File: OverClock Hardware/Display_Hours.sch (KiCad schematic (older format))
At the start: 41 parts

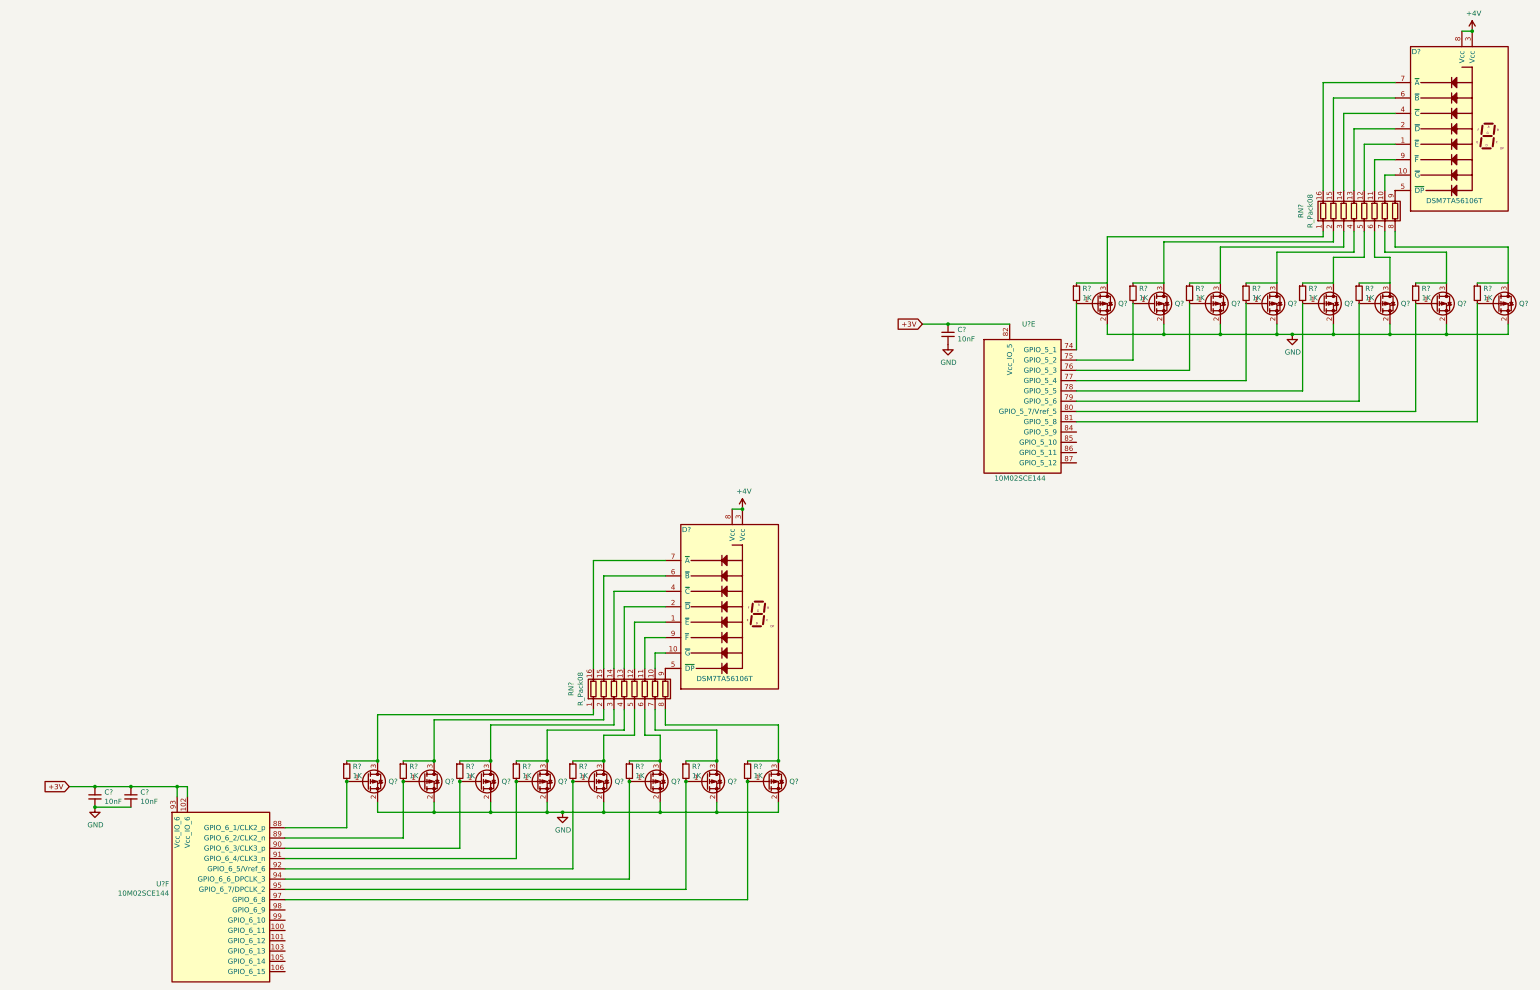
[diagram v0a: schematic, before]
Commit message: Interfaced minutes digits to FPGA and added time selection methods
Interfaced the two 7 Segment displays used for displaying the minutes to the FPGA. 

Added 4 Tactile switches to increment/decrement the hours and minutes separately.

Added a header to allow for setting of the time via UART.
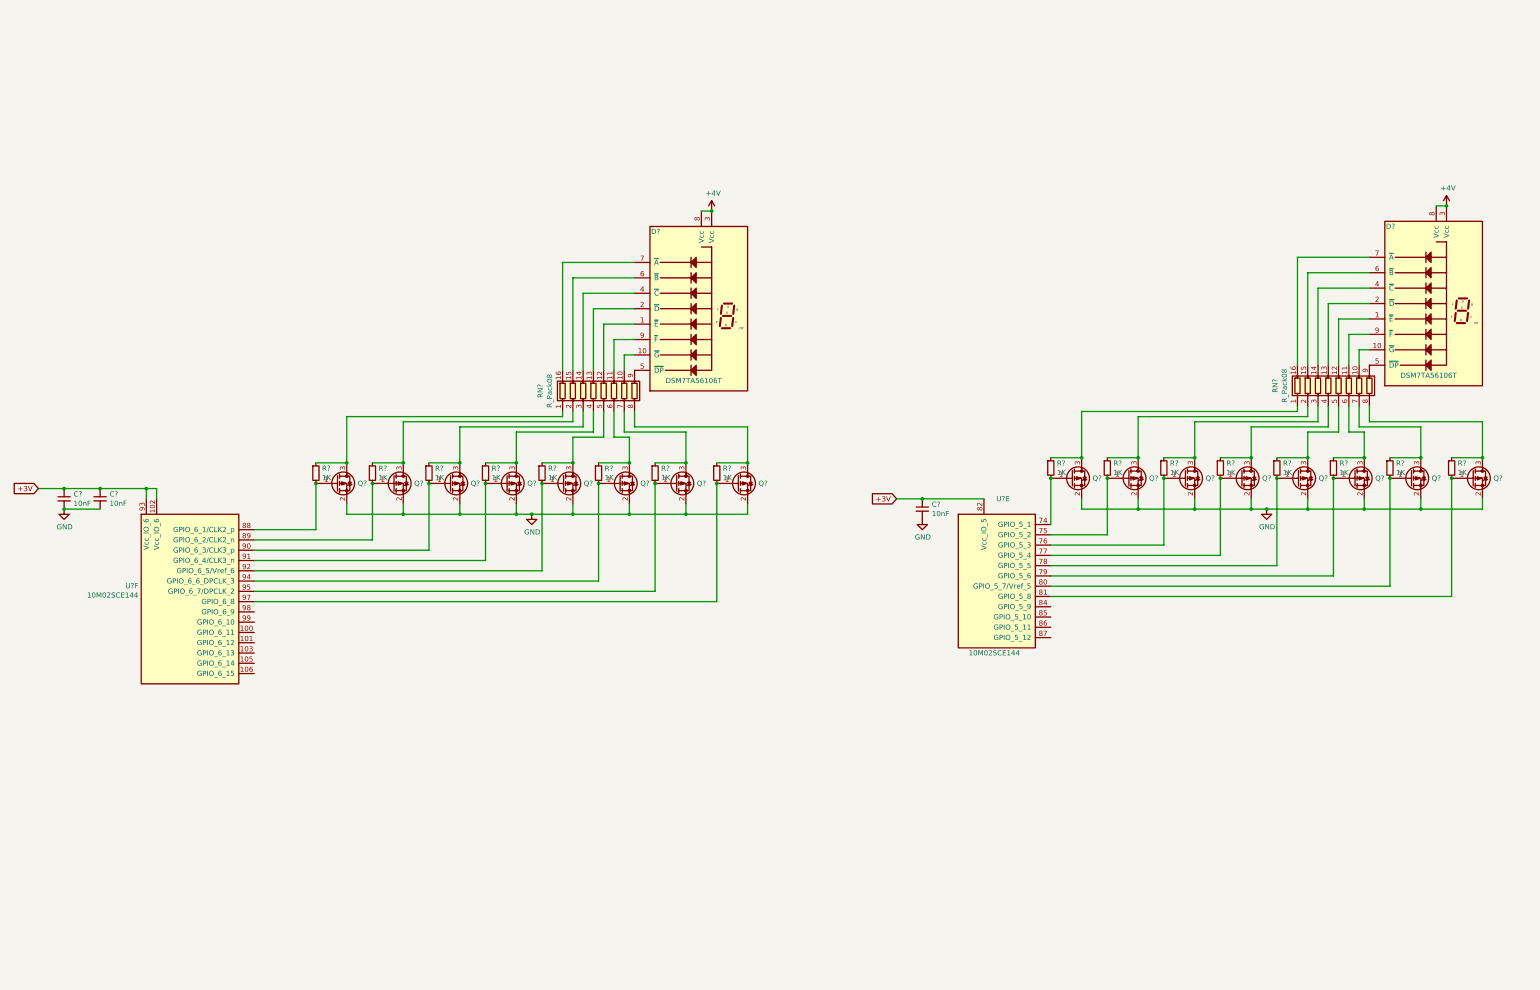
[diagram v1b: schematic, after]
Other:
- moved on the sheet: C?, D?, Q?, R?, RN?, U?E, U?F

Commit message: Completed Schematic and ran ERC
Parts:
- gave numbers to parts that had none: 40
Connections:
- no-connect marks 0 -> 11

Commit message: Matched symbols to footprints and generated netlist
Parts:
- D1, D2: footprint (none) -> Maxted Libs:DSM7TA56106T
- R11, R12, R13, R14, R15, R16, R17, R18, R19, R20, R21, R22, R23, R24, R25, R26: footprint (none) -> Resistor_SMD:R_0805_2012Metric_Pad1.15x1.40mm_HandSolder
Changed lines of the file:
@@
 F 0 "D1" H 14200 4550 50  0000 R CNN
 F 1 "DSM7TA56106T" H 14800 3100 50  0000 R CNN
-F 2 "" H 14900 3750 50  0001 C CNN
+F 2 "Maxted Libs:DSM7TA56106T" H 14900 3750 50  0001 C CNN
 F 3 "" H 14900 3750 50  0001 C CNN
 	1    14600 3750
@@
 F 0 "R11" H 10909 5346 50  0000 L CNN
 F 1 "1K" H 10909 5255 50  0000 L CNN
-F 2 "" H 10850 5300 50  0001 C CNN
+F 2 "Resistor_SMD:R_0805_2012Metric_Pad1.15x1.40mm_HandSolder" H 10850 5300 50  0001 C CNN
 F 3 "~" H 10850 5300 50  0001 C CNN
 	1    10850 5300
@@
 F 0 "R12" H 11459 5346 50  0000 L CNN
 F 1 "1K" H 11459 5255 50  0000 L CNN
-F 2 "" H 11400 5300 50  0001 C CNN
+F 2 "Resistor_SMD:R_0805_2012Metric_Pad1.15x1.40mm_HandSolder" H 11400 5300 50  0001 C CNN
 F 3 "~" H 11400 5300 50  0001 C CNN
 	1    11400 5300
@@
 F 0 "R13" H 12009 5346 50  0000 L CNN
 F 1 "1K" H 12009 5255 50  0000 L CNN
-F 2 "" H 11950 5300 50  0001 C CNN
+F 2 "Resistor_SMD:R_0805_2012Metric_Pad1.15x1.40mm_HandSolder" H 11950 5300 50  0001 C CNN
 F 3 "~" H 11950 5300 50  0001 C CNN
 	1    11950 5300
@@
 F 0 "R14" H 12559 5346 50  0000 L CNN
 F 1 "1K" H 12559 5255 50  0000 L CNN
-F 2 "" H 12500 5300 50  0001 C CNN
+F 2 "Resistor_SMD:R_0805_2012Metric_Pad1.15x1.40mm_HandSolder" H 12500 5300 50  0001 C CNN
 F 3 "~" H 12500 5300 50  0001 C CNN
 	1    12500 5300
@@
 F 0 "R15" H 13109 5346 50  0000 L CNN
 F 1 "1K" H 13109 5255 50  0000 L CNN
-F 2 "" H 13050 5300 50  0001 C CNN
+F 2 "Resistor_SMD:R_0805_2012Metric_Pad1.15x1.40mm_HandSolder" H 13050 5300 50  0001 C CNN
 F 3 "~" H 13050 5300 50  0001 C CNN
 	1    13050 5300
@@
 F 0 "R16" H 13659 5346 50  0000 L CNN
 F 1 "1K" H 13659 5255 50  0000 L CNN
-F 2 "" H 13600 5300 50  0001 C CNN
+F 2 "Resistor_SMD:R_0805_2012Metric_Pad1.15x1.40mm_HandSolder" H 13600 5300 50  0001 C CNN
 F 3 "~" H 13600 5300 50  0001 C CNN
 	1    13600 5300
@@
 F 0 "R17" H 14209 5346 50  0000 L CNN
 F 1 "1K" H 14209 5255 50  0000 L CNN
-F 2 "" H 14150 5300 50  0001 C CNN
+F 2 "Resistor_SMD:R_0805_2012Metric_Pad1.15x1.40mm_HandSolder" H 14150 5300 50  0001 C CNN
 F 3 "~" H 14150 5300 50  0001 C CNN
 	1    14150 5300
@@
 F 0 "R18" H 14809 5346 50  0000 L CNN
 F 1 "1K" H 14809 5255 50  0000 L CNN
-F 2 "" H 14750 5300 50  0001 C CNN
+F 2 "Resistor_SMD:R_0805_2012Metric_Pad1.15x1.40mm_HandSolder" H 14750 5300 50  0001 C CNN
 F 3 "~" H 14750 5300 50  0001 C CNN
 	1    14750 5300
@@
 F 0 "D2" H 7050 4600 50  0000 R CNN
 F 1 "DSM7TA56106T" H 7650 3150 50  0000 R CNN
-F 2 "" H 7750 3800 50  0001 C CNN
+F 2 "Maxted Libs:DSM7TA56106T" H 7750 3800 50  0001 C CNN
 F 3 "" H 7750 3800 50  0001 C CNN
 	1    7450 3800
@@
 F 0 "R19" H 3759 5396 50  0000 L CNN
 F 1 "1K" H 3759 5305 50  0000 L CNN
-F 2 "" H 3700 5350 50  0001 C CNN
+F 2 "Resistor_SMD:R_0805_2012Metric_Pad1.15x1.40mm_HandSolder" H 3700 5350 50  0001 C CNN
 F 3 "~" H 3700 5350 50  0001 C CNN
 	1    3700 5350
@@
 F 0 "R20" H 4309 5396 50  0000 L CNN
 F 1 "1K" H 4309 5305 50  0000 L CNN
-F 2 "" H 4250 5350 50  0001 C CNN
+F 2 "Resistor_SMD:R_0805_2012Metric_Pad1.15x1.40mm_HandSolder" H 4250 5350 50  0001 C CNN
 F 3 "~" H 4250 5350 50  0001 C CNN
 	1    4250 5350
@@
 F 0 "R21" H 4859 5396 50  0000 L CNN
 F 1 "1K" H 4859 5305 50  0000 L CNN
-F 2 "" H 4800 5350 50  0001 C CNN
+F 2 "Resistor_SMD:R_0805_2012Metric_Pad1.15x1.40mm_HandSolder" H 4800 5350 50  0001 C CNN
 F 3 "~" H 4800 5350 50  0001 C CNN
 	1    4800 5350
@@
 F 0 "R22" H 5409 5396 50  0000 L CNN
 F 1 "1K" H 5409 5305 50  0000 L CNN
-F 2 "" H 5350 5350 50  0001 C CNN
+F 2 "Resistor_SMD:R_0805_2012Metric_Pad1.15x1.40mm_HandSolder" H 5350 5350 50  0001 C CNN
 F 3 "~" H 5350 5350 50  0001 C CNN
 	1    5350 5350
@@
 F 0 "R23" H 5959 5396 50  0000 L CNN
 F 1 "1K" H 5959 5305 50  0000 L CNN
-F 2 "" H 5900 5350 50  0001 C CNN
+F 2 "Resistor_SMD:R_0805_2012Metric_Pad1.15x1.40mm_HandSolder" H 5900 5350 50  0001 C CNN
 F 3 "~" H 5900 5350 50  0001 C CNN
 	1    5900 5350
@@
 F 0 "R24" H 6509 5396 50  0000 L CNN
 F 1 "1K" H 6509 5305 50  0000 L CNN
-F 2 "" H 6450 5350 50  0001 C CNN
+F 2 "Resistor_SMD:R_0805_2012Metric_Pad1.15x1.40mm_HandSolder" H 6450 5350 50  0001 C CNN
 F 3 "~" H 6450 5350 50  0001 C CNN
 	1    6450 5350
@@
 F 0 "R25" H 7059 5396 50  0000 L CNN
 F 1 "1K" H 7059 5305 50  0000 L CNN
-F 2 "" H 7000 5350 50  0001 C CNN
+F 2 "Resistor_SMD:R_0805_2012Metric_Pad1.15x1.40mm_HandSolder" H 7000 5350 50  0001 C CNN
 F 3 "~" H 7000 5350 50  0001 C CNN
 	1    7000 5350
@@
 F 0 "R26" H 7659 5396 50  0000 L CNN
 F 1 "1K" H 7659 5305 50  0000 L CNN
-F 2 "" H 7600 5350 50  0001 C CNN
+F 2 "Resistor_SMD:R_0805_2012Metric_Pad1.15x1.40mm_HandSolder" H 7600 5350 50  0001 C CNN
 F 3 "~" H 7600 5350 50  0001 C CNN
 	1    7600 5350

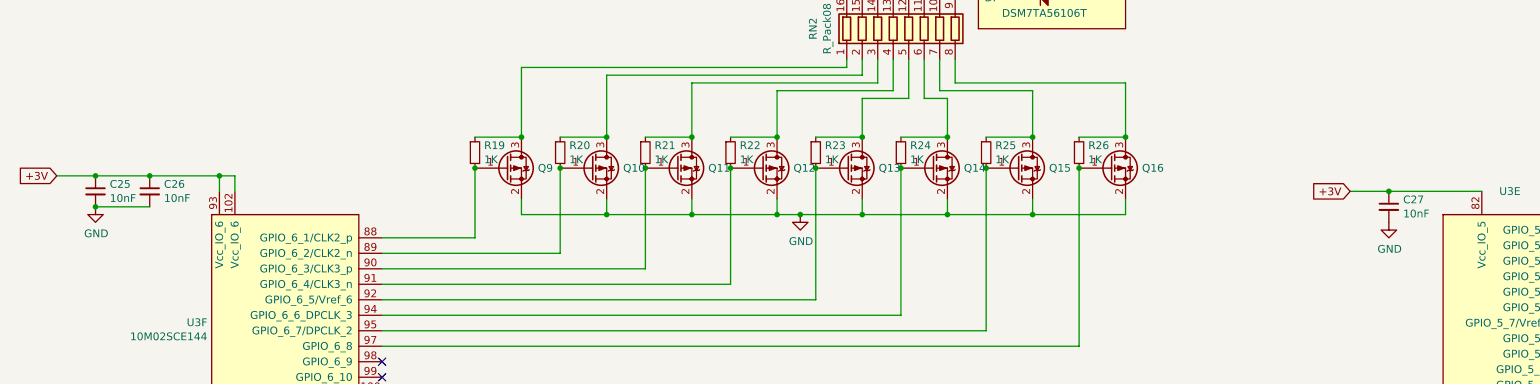
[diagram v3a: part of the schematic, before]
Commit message: Place and route Decoupling Capacitors
Placed and routed all the decoupling capacitors for the FPGA. Created Top and bottom GND planes too for better signal integrity
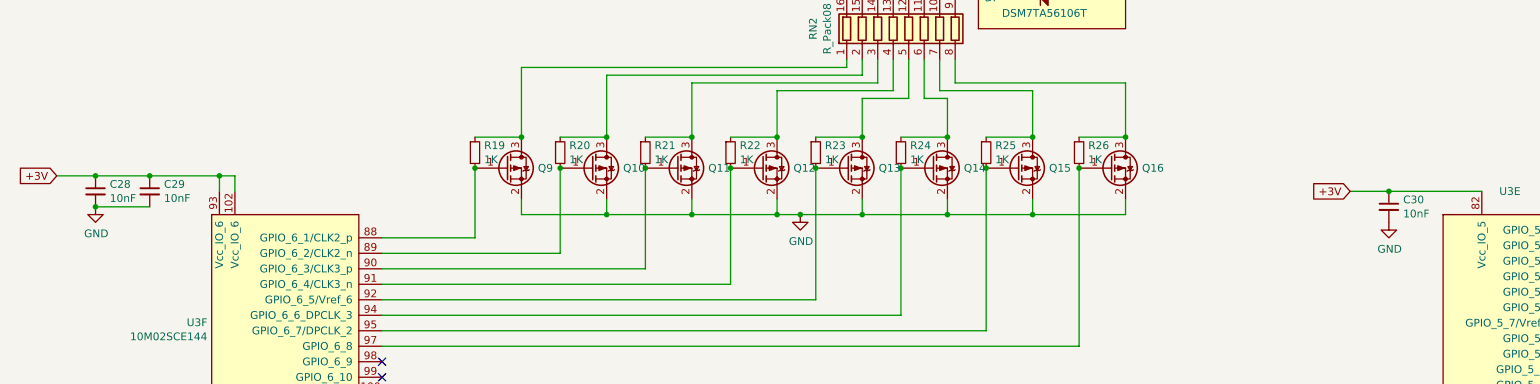
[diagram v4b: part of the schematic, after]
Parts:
- C28: renamed from C25; footprint Capacitor_SMD:C_0805_2012Metric_Pad1.15x1.40mm_HandSolder -> Capacitor_SMD:C_0603_1608Metric_Pad1.05x0.95mm_HandSolder
- C29: renamed from C26; footprint Capacitor_SMD:C_0805_2012Metric_Pad1.15x1.40mm_HandSolder -> Capacitor_SMD:C_0603_1608Metric_Pad1.05x0.95mm_HandSolder
- C30: renamed from C27; footprint Capacitor_SMD:C_0805_2012Metric_Pad1.15x1.40mm_HandSolder -> Capacitor_SMD:C_0603_1608Metric_Pad1.05x0.95mm_HandSolder
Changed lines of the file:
@@
 AR Path="/5C88C7E9" Ref="#PWR?"  Part="1"
 AR Path="/5C66B7E8/5C88C7E9" Ref="#PWR?"  Part="1"
-AR Path="/5C87E0ED/5C88C7E9" Ref="#PWR012"  Part="1"
-F 0 "#PWR012" H 14700 2600 50  0001 C CNN
+AR Path="/5C87E0ED/5C88C7E9" Ref="#PWR013"  Part="1"
+F 0 "#PWR013" H 14700 2600 50  0001 C CNN
 F 1 "+4V" H 14715 2923 50  0000 C CNN
 F 2 "" H 14700 2750 50  0001 C CNN
@@
 P 12950 5700
 AR Path="/5C66B7E8/5C88C84E" Ref="#PWR?"  Part="1"
-AR Path="/5C87E0ED/5C88C84E" Ref="#PWR015"  Part="1"
-F 0 "#PWR015" H 12950 5450 50  0001 C CNN
+AR Path="/5C87E0ED/5C88C84E" Ref="#PWR016"  Part="1"
+F 0 "#PWR016" H 12950 5450 50  0001 C CNN
 F 1 "GND" H 12955 5527 50  0000 C CNN
 F 2 "" H 12950 5700 50  0001 C CNN
@@
 AR Path="/5C8E1836" Ref="#PWR?"  Part="1"
 AR Path="/5C66B7E8/5C8E1836" Ref="#PWR?"  Part="1"
-AR Path="/5C87E0ED/5C8E1836" Ref="#PWR013"  Part="1"
-F 0 "#PWR013" H 7550 2650 50  0001 C CNN
+AR Path="/5C87E0ED/5C8E1836" Ref="#PWR014"  Part="1"
+F 0 "#PWR014" H 7550 2650 50  0001 C CNN
 F 1 "+4V" H 7565 2973 50  0000 C CNN
 F 2 "" H 7550 2800 50  0001 C CNN
@@
 P 5800 5750
 AR Path="/5C66B7E8/5C8E1893" Ref="#PWR?"  Part="1"
-AR Path="/5C87E0ED/5C8E1893" Ref="#PWR016"  Part="1"
-F 0 "#PWR016" H 5800 5500 50  0001 C CNN
+AR Path="/5C87E0ED/5C8E1893" Ref="#PWR017"  Part="1"
+F 0 "#PWR017" H 5800 5500 50  0001 C CNN
 F 1 "GND" H 5805 5577 50  0000 C CNN
 F 2 "" H 5800 5750 50  0001 C CNN
@@
 $EndComp
 $Comp
-L Device:C_Small C26
+L Device:C_Small C29
 U 1 1 5C98C1FA
 P 1600 5600
-F 0 "C26" H 1692 5646 50  0000 L CNN
+F 0 "C29" H 1692 5646 50  0000 L CNN
 F 1 "10nF" H 1692 5555 50  0000 L CNN
-F 2 "Capacitor_SMD:C_0805_2012Metric_Pad1.15x1.40mm_HandSolder" H 1600 5600 50  0001 C CNN
+F 2 "Capacitor_SMD:C_0603_1608Metric_Pad1.05x0.95mm_HandSolder" H 1600 5600 50  0001 C CNN
 F 3 "~" H 1600 5600 50  0001 C CNN
 	1    1600 5600
@@
 $EndComp
 $Comp
-L Device:C_Small C25
+L Device:C_Small C28
 U 1 1 5C98C3B4
 P 1250 5600
-F 0 "C25" H 1342 5646 50  0000 L CNN
+F 0 "C28" H 1342 5646 50  0000 L CNN
 F 1 "10nF" H 1342 5555 50  0000 L CNN
-F 2 "Capacitor_SMD:C_0805_2012Metric_Pad1.15x1.40mm_HandSolder" H 1250 5600 50  0001 C CNN
+F 2 "Capacitor_SMD:C_0603_1608Metric_Pad1.05x0.95mm_HandSolder" H 1250 5600 50  0001 C CNN
 F 3 "~" H 1250 5600 50  0001 C CNN
 	1    1250 5600
@@
 	1600 5700 1250 5700
 $Comp
-L power:GND #PWR014
+L power:GND #PWR015
 U 1 1 5C9A722E
 P 1250 5700
-F 0 "#PWR014" H 1250 5450 50  0001 C CNN
+F 0 "#PWR015" H 1250 5450 50  0001 C CNN
 F 1 "GND" H 1255 5527 50  0000 C CNN
 F 2 "" H 1250 5700 50  0001 C CNN
@@
 Connection ~ 1250 5700
 $Comp
-L Device:C_Small C27
+L Device:C_Small C30
 U 1 1 5C9A89C4
 P 9600 5700
-F 0 "C27" H 9692 5746 50  0000 L CNN
+F 0 "C30" H 9692 5746 50  0000 L CNN
 F 1 "10nF" H 9692 5655 50  0000 L CNN
-F 2 "Capacitor_SMD:C_0805_2012Metric_Pad1.15x1.40mm_HandSolder" H 9600 5700 50  0001 C CNN
+F 2 "Capacitor_SMD:C_0603_1608Metric_Pad1.05x0.95mm_HandSolder" H 9600 5700 50  0001 C CNN
 F 3 "~" H 9600 5700 50  0001 C CNN
 	1    9600 5700
@@
 $EndComp
 $Comp
-L power:GND #PWR017
+L power:GND #PWR018
 U 1 1 5C9B1C90
 P 9600 5800
-F 0 "#PWR017" H 9600 5550 50  0001 C CNN
+F 0 "#PWR018" H 9600 5550 50  0001 C CNN
 F 1 "GND" H 9605 5627 50  0000 C CNN
 F 2 "" H 9600 5800 50  0001 C CNN
